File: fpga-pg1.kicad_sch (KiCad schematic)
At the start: 1 part, among them U1 XC7A15T-FTG256

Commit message: more stuff
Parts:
- added R11, R12, R13, R14, R15: 0, Resistor_SMD:R_0402_1005Metric_Pad0.72x0.64mm_HandSolder, symbol Device:R
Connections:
- net INT_FLASH_SPI_D0: now reaches U1.J13 (IO_L1P_T0_D00_MOSI_14)
- net INT_FLASH_SPI_D0: now also R11.2
- net INT_FLASH_SPI_D1: now reaches U1.J14 (IO_L1N_T0_D01_DIN_14)
- net INT_FLASH_SPI_D1: now also R12.2
- net INT_FLASH_SPI_D2: now reaches U1.K15 (IO_L2P_T0_D02_14)
- net INT_FLASH_SPI_D2: now also R13.2
- net INT_FLASH_SPI_D3: now reaches U1.K16 (IO_L2N_T0_D03_14)
- net INT_FLASH_SPI_D3: now also R14.2
- net INT_FLASH_SPI_CS#: now reaches U1.L12 (IO_L6P_T0_FCS_B_14)
- net INT_FLASH_SPI_CS#: now also R15.2
- new net FLASH_SPI.CS#: R15.1
- new net FLASH_SPI.D0: R11.1
- new net FLASH_SPI.D1: R12.1
- new net FLASH_SPI.D2: R13.1
- new net FLASH_SPI.D3: R14.1

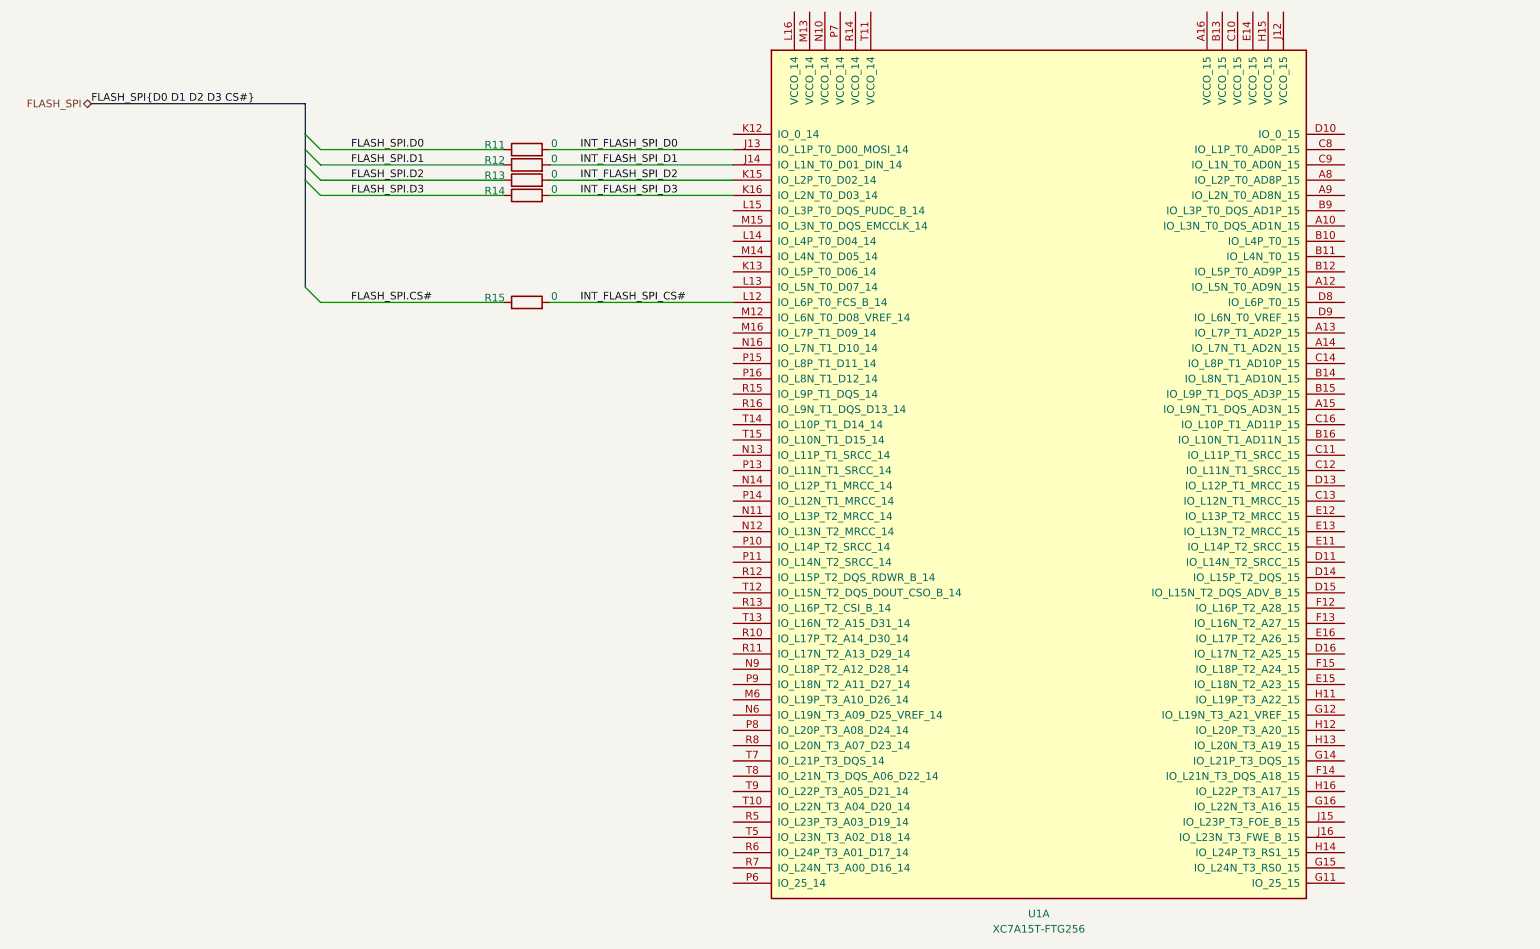
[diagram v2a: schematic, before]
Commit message: changed ftg256 to csg325, wanted xc7a12t but couldnt find
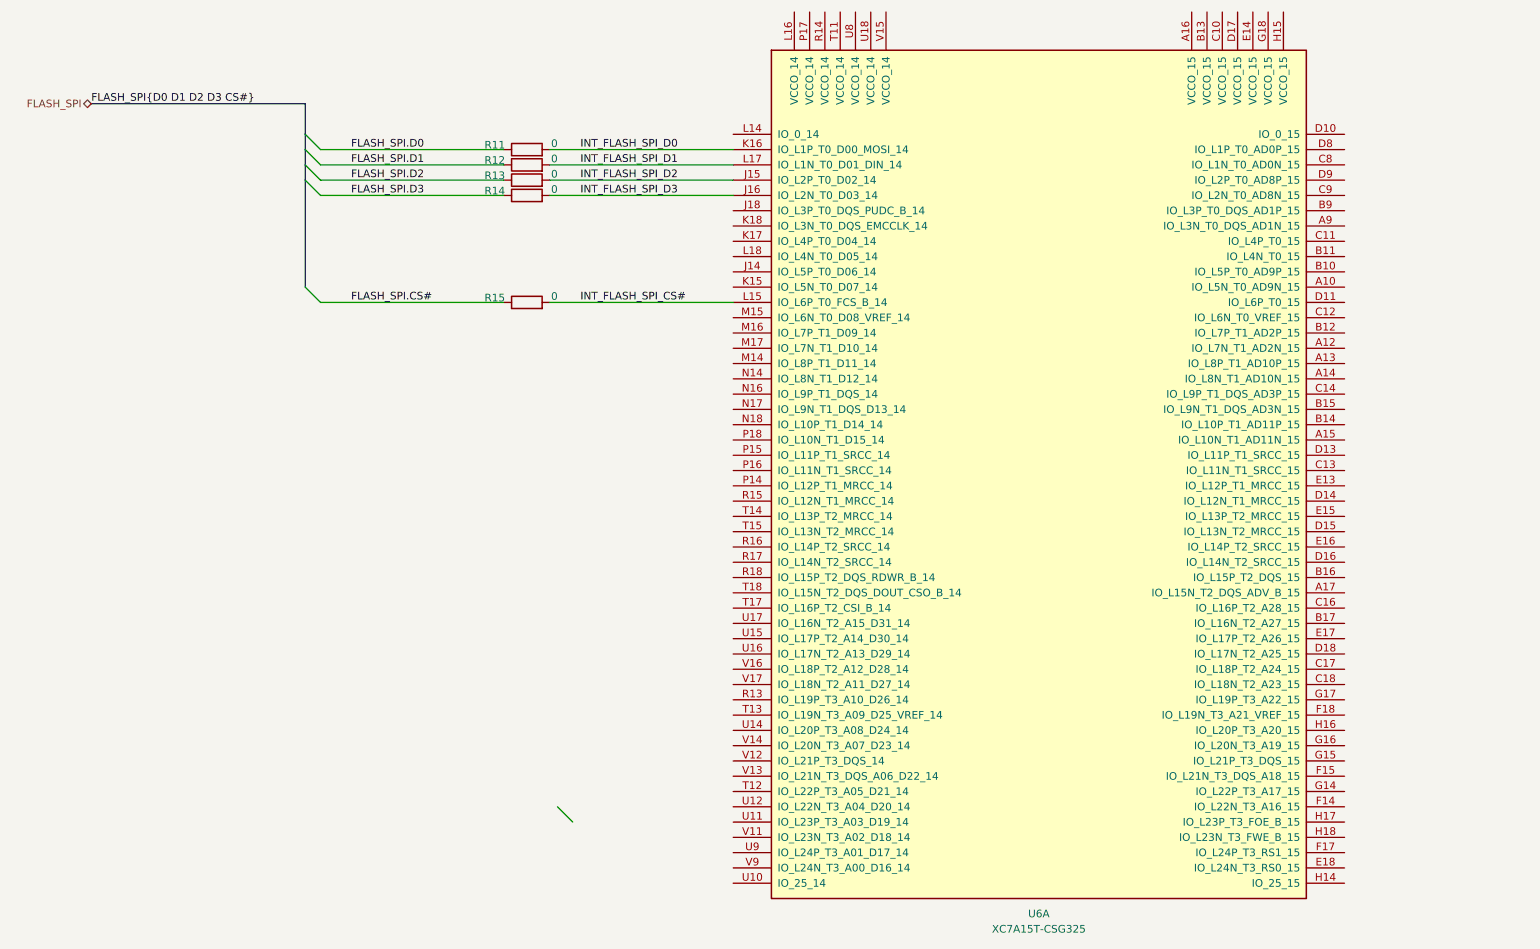
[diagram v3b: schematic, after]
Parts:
- removed U1: XC7A15T-FTG256, Package_BGA:Xilinx_FTG256, symbol FPGA_Xilinx_Artix7:XC7A15T-FTG256
- added U6: XC7A15T-CSG325, Package_BGA:Xilinx_CSG325, symbol FPGA_Xilinx_Artix7:XC7A15T-CSG325
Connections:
- net INT_FLASH_SPI_CS#: now also U6.L15 (IO_L6P_T0_FCS_B_14)
- net INT_FLASH_SPI_D0: now also U6.K16 (IO_L1P_T0_D00_MOSI_14)
- net INT_FLASH_SPI_D1: now also U6.L17 (IO_L1N_T0_D01_DIN_14)
- net INT_FLASH_SPI_D2: now also U6.J15 (IO_L2P_T0_D02_14)
- net INT_FLASH_SPI_D3: now also U6.J16 (IO_L2N_T0_D03_14)

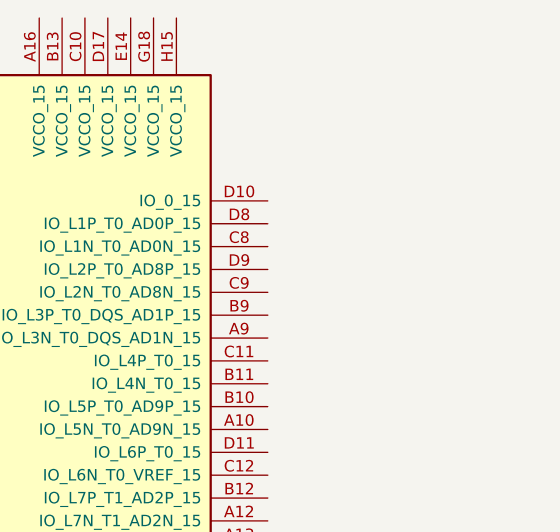
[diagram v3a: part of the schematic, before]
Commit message: started mapping data input pins
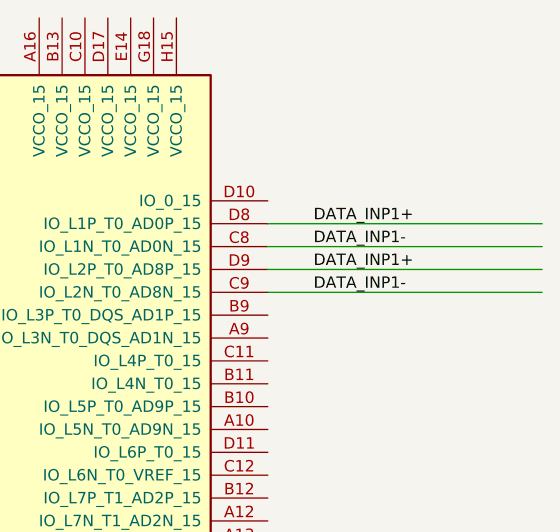
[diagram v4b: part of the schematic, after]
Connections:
- net DATA_INP1-: now reaches U6.C8 (IO_L1N_T0_AD0N_15)
- net DATA_INP1-: now also U6.C9 (IO_L2N_T0_AD8N_15)
- net DATA_INP1+: now reaches U6.D8 (IO_L1P_T0_AD0P_15)
- net DATA_INP1+: now also U6.D9 (IO_L2P_T0_AD8P_15)
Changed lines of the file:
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@@
+	(wire
+		(pts
+			(xy 270.51 87.63) (xy 300.99 87.63)
+		)
+		(stroke
+			(width 0)
+			(type default)
+		)
+	)
 	(wire
 		(pts
@@
 	(wire
 		(pts
+			(xy 270.51 95.25) (xy 300.99 95.25)
+		)
+		(stroke
+			(width 0)
+			(type default)
+		)
+	)
+	(wire
+		(pts
 			(xy 138.43 113.03) (xy 168.91 113.03)
 		)
@@
 	(wire
 		(pts
+			(xy 270.51 90.17) (xy 300.99 90.17)
+		)
+		(stroke
+			(width 0)
+			(type default)
+		)
+	)
+	(wire
+		(pts
 			(xy 138.43 87.63) (xy 168.91 87.63)
+		)
+		(stroke
+			(width 0)
+			(type default)
+		)
+	)
+	(wire
+		(pts
+			(xy 270.51 92.71) (xy 300.99 92.71)
 		)
 		(stroke
@@
 		)
 	)
+	(label "DATA_INP1+"
+		(at 275.59 87.63 0)
+		(fields_autoplaced yes)
+		(effects
+			(font
+				(size 1.27 1.27)
+			)
+			(justify left bottom)
+		)
+	)
+	(label "DATA_INP1-"
+		(at 275.59 95.25 0)
+		(fields_autoplaced yes)
+		(effects
+			(font
+				(size 1.27 1.27)
+			)
+			(justify left bottom)
+		)
+	)
 	(label "INT_FLASH_SPI_D1"
 		(at 143.51 90.17 0)
@@
 		)
 	)
+	(label "DATA_INP1-"
+		(at 275.59 90.17 0)
+		(fields_autoplaced yes)
+		(effects
+			(font
+				(size 1.27 1.27)
+			)
+			(justify left bottom)
+		)
+	)
 	(label "FLASH_SPI.D3"
 		(at 105.41 95.25 0)
@@
 		(fields_autoplaced yes)
 		(effects
+			(font
+				(size 1.27 1.27)
+			)
+			(justify left bottom)
+		)
+	)
+	(label "DATA_INP1+"
+		(at 275.59 92.71 0)
+		(fields_autoplaced yes)
+		(effects

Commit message: stuff
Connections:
- net DATA_INP1+: now also U6.C17 (IO_L18P_T2_A24_15), U6.E17 (IO_L17P_T2_A26_15), U6.F17 (IO_L24P_T3_RS1_15), U6.G14 (IO_L22P_T3_A17_15), U6.G15 (IO_L21P_T3_DQS_15), U6.G17 (IO_L19P_T3_A22_15), U6.H16 (IO_L20P_T3_A20_15), U6.H17 (IO_L23P_T3_FOE_B_15); no longer U6.D9 (IO_L2P_T0_AD8P_15)
- net DATA_INP1-: now also U6.C18 (IO_L18N_T2_A23_15), U6.D18 (IO_L17N_T2_A25_15), U6.E18 (IO_L24N_T3_RS0_15), U6.F14 (IO_L22N_T3_A16_15), U6.F15 (IO_L21N_T3_DQS_A18_15), U6.F18 (IO_L19N_T3_A21_VREF_15), U6.G16 (IO_L20N_T3_A19_15), U6.H18 (IO_L23N_T3_FWE_B_15); no longer U6.C9 (IO_L2N_T0_AD8N_15)
- net DATA_INP5-: now reaches U6.A10 (IO_L5N_T0_AD9N_15)
- net DATA_INP7-: now reaches U6.A12 (IO_L7N_T1_AD2N_15)
- net DATA_INP8+: now reaches U6.A13 (IO_L8P_T1_AD10P_15)
- net DATA_INP8-: now reaches U6.A14 (IO_L8N_T1_AD10N_15)
- net DATA_INP10-: now reaches U6.A15 (IO_L10N_T1_AD11N_15)
- net DATA_INP15-: now reaches U6.A17 (IO_L15N_T2_DQS_ADV_B_15)
- net DATA_INP3-: now reaches U6.A9 (IO_L3N_T0_DQS_AD1N_15)
- net DATA_INP5+: now reaches U6.B10 (IO_L5P_T0_AD9P_15)
- net DATA_INP4-: now reaches U6.B11 (IO_L4N_T0_15)
- net DATA_INP7+: now reaches U6.B12 (IO_L7P_T1_AD2P_15)
- net DATA_INP10+: now reaches U6.B14 (IO_L10P_T1_AD11P_15)
- net DATA_INP9-: now reaches U6.B15 (IO_L9N_T1_DQS_AD3N_15)
- net DATA_INP15+: now reaches U6.B16 (IO_L15P_T2_DQS_15)
- net DATA_INP16-: now reaches U6.B17 (IO_L16N_T2_A27_15)
- net DATA_INP3+: now reaches U6.B9 (IO_L3P_T0_DQS_AD1P_15)
- net DATA_INP4+: now reaches U6.C11 (IO_L4P_T0_15)
- net DATA_INP6-: now reaches U6.C12 (IO_L6N_T0_VREF_15)
- net DATA_INP11-: now reaches U6.C13 (IO_L11N_T1_SRCC_15)
- net DATA_INP9+: now reaches U6.C14 (IO_L9P_T1_DQS_AD3P_15)
- net DATA_INP16+: now reaches U6.C16 (IO_L16P_T2_A28_15)
- net DATA_INP6+: now reaches U6.D11 (IO_L6P_T0_15)
- net DATA_INP11+: now reaches U6.D13 (IO_L11P_T1_SRCC_15)
- net DATA_INP12-: now reaches U6.D14 (IO_L12N_T1_MRCC_15)
- net DATA_INP13-: now reaches U6.D15 (IO_L13N_T2_MRCC_15)
- net DATA_INP14-: now reaches U6.D16 (IO_L14N_T2_SRCC_15)
- net DATA_INP12+: now reaches U6.E13 (IO_L12P_T1_MRCC_15)
- net DATA_INP13+: now reaches U6.E15 (IO_L13P_T2_MRCC_15)
- net DATA_INP14+: now reaches U6.E16 (IO_L14P_T2_SRCC_15)
- new net DATA_INP2+: U6.D9 (IO_L2P_T0_AD8P_15)
- new net DATA_INP2-: U6.C9 (IO_L2N_T0_AD8N_15)

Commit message: stuff
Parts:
- added TP17, TP18, TP19, TP20, TP21, TP22, TP23, TP24, TP25, TP26, TP27, TP28, TP29, TP30, TP31, TP32, TP33, TP34, TP35, TP36, TP37, TP38, TP39, TP40, TP41, TP42, TP43, TP44, TP45, TP46, TP47, TP48: TestPoint_Small, symbol Connector:TestPoint_Small
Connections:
- net DATA_INP1+: no longer U6.C17 (IO_L18P_T2_A24_15), U6.E17 (IO_L17P_T2_A26_15), U6.F17 (IO_L24P_T3_RS1_15), U6.G14 (IO_L22P_T3_A17_15), U6.G15 (IO_L21P_T3_DQS_15), U6.G17 (IO_L19P_T3_A22_15), U6.H16 (IO_L20P_T3_A20_15), U6.H17 (IO_L23P_T3_FOE_B_15)
- net DATA_INP1-: no longer U6.C18 (IO_L18N_T2_A23_15), U6.D18 (IO_L17N_T2_A25_15), U6.E18 (IO_L24N_T3_RS0_15), U6.F14 (IO_L22N_T3_A16_15), U6.F15 (IO_L21N_T3_DQS_A18_15), U6.F18 (IO_L19N_T3_A21_VREF_15), U6.G16 (IO_L20N_T3_A19_15), U6.H18 (IO_L23N_T3_FWE_B_15)
- net DO.DO3+: now reaches U6.J14 (IO_L5P_T0_D06_14)
- net DO.DO3+: now also TP21.1
- net DO.DO1+: now reaches U6.J18 (IO_L3P_T0_DQS_PUDC_B_14)
- net DO.DO1+: now also TP17.1
- net DO.DO3-: now reaches U6.K15 (IO_L5N_T0_D07_14)
- net DO.DO3-: now also TP22.1
- net DO.DO2+: now reaches U6.K17 (IO_L4P_T0_D04_14)
- net DO.DO2+: now also TP19.1
- net DO.DO1-: now reaches U6.K18 (IO_L3N_T0_DQS_EMCCLK_14)
- net DO.DO1-: now also TP18.1
- net DO.DO2-: now reaches U6.L18 (IO_L4N_T0_D05_14)
- net DO.DO2-: now also TP20.1
- net DO.DO5+: now reaches U6.M14 (IO_L8P_T1_D11_14)
- net DO.DO5+: now also TP25.1
- net DO.DO4+: now reaches U6.M16 (IO_L7P_T1_D09_14)
- net DO.DO4+: now also TP23.1
- net DO.DO4-: now reaches U6.M17 (IO_L7N_T1_D10_14)
- net DO.DO4-: now also TP24.1
- net DO.DO5-: now reaches U6.N14 (IO_L8N_T1_D12_14)
- net DO.DO5-: now also TP26.1
- net DO.DO6+: now reaches U6.N16 (IO_L9P_T1_DQS_14)
- net DO.DO6+: now also TP27.1
- net DO.DO6-: now reaches U6.N17 (IO_L9N_T1_DQS_D13_14)
- net DO.DO6-: now also TP28.1
- net DO.DO7+: now reaches U6.N18 (IO_L10P_T1_D14_14)
- net DO.DO7+: now also TP29.1
- net DO.DO9+: now reaches U6.P14 (IO_L12P_T1_MRCC_14)
- net DO.DO9+: now also TP33.1
- net DO.DO8+: now reaches U6.P15 (IO_L11P_T1_SRCC_14)
- net DO.DO8+: now also TP31.1
- net DO.DO8-: now reaches U6.P16 (IO_L11N_T1_SRCC_14)
- net DO.DO8-: now also TP32.1
- net DO.DO7-: now reaches U6.P18 (IO_L10N_T1_D15_14)
- net DO.DO7-: now also TP30.1
- net DO.DO16+: now reaches U6.R13 (IO_L19P_T3_A10_D26_14)
- net DO.DO16+: now also TP47.1
- net DO.DO9-: now reaches U6.R15 (IO_L12N_T1_MRCC_14)
- net DO.DO9-: now also TP34.1
- net DO.DO11+: now reaches U6.R16 (IO_L14P_T2_SRCC_14)
- net DO.DO11+: now also TP37.1
- net DO.DO11-: now reaches U6.R17 (IO_L14N_T2_SRCC_14)
- net DO.DO11-: now also TP38.1
- net DO.DO12+: now reaches U6.R18 (IO_L15P_T2_DQS_RDWR_B_14)
- net DO.DO12+: now also TP39.1
- net DO.DO16-: now reaches U6.T13 (IO_L19N_T3_A09_D25_VREF_14)
- net DO.DO16-: now also TP48.1
- net DO.DO10+: now reaches U6.T14 (IO_L13P_T2_MRCC_14)
- net DO.DO10+: now also TP35.1
- net DO.DO10-: now reaches U6.T15 (IO_L13N_T2_MRCC_14)
- net DO.DO10-: now also TP36.1
- net DO.DO13+: now reaches U6.T17 (IO_L16P_T2_CSI_B_14)
- net DO.DO13+: now also TP41.1
- net DO.DO12-: now reaches U6.T18 (IO_L15N_T2_DQS_DOUT_CSO_B_14)
- net DO.DO12-: now also TP40.1
- net DO.DO14+: now reaches U6.U15 (IO_L17P_T2_A14_D30_14)
- net DO.DO14+: now also TP43.1
- net DO.DO14-: now reaches U6.U16 (IO_L17N_T2_A13_D29_14)
- net DO.DO14-: now also TP44.1
- net DO.DO13-: now reaches U6.U17 (IO_L16N_T2_A15_D31_14)
- net DO.DO13-: now also TP42.1
- net DO.DO15+: now reaches U6.V16 (IO_L18P_T2_A12_D28_14)
- net DO.DO15+: now also TP45.1
- net DO.DO15-: now reaches U6.V17 (IO_L18N_T2_A11_D27_14)
- net DO.DO15-: now also TP46.1
